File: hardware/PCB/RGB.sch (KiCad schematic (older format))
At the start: 26 parts, among them U1 IS31FL3733-QF, U2 IS31FL3733-QF

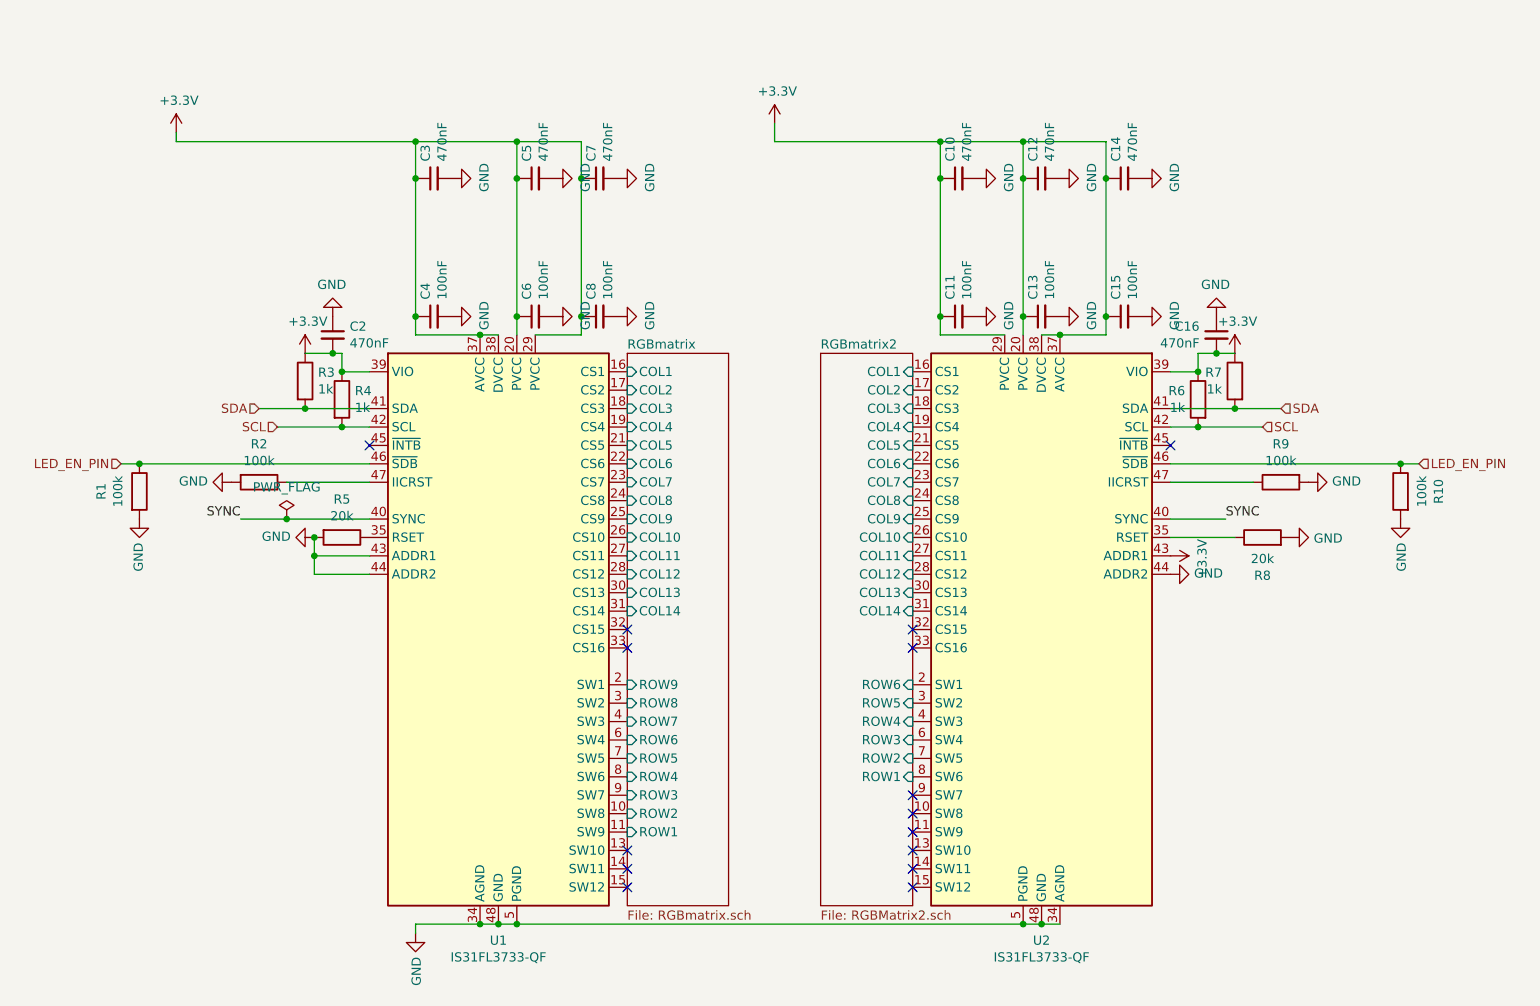
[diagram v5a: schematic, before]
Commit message: Use the correct Footprint
I think I can't do more things before the parts arrive and figure out what LED im going to use
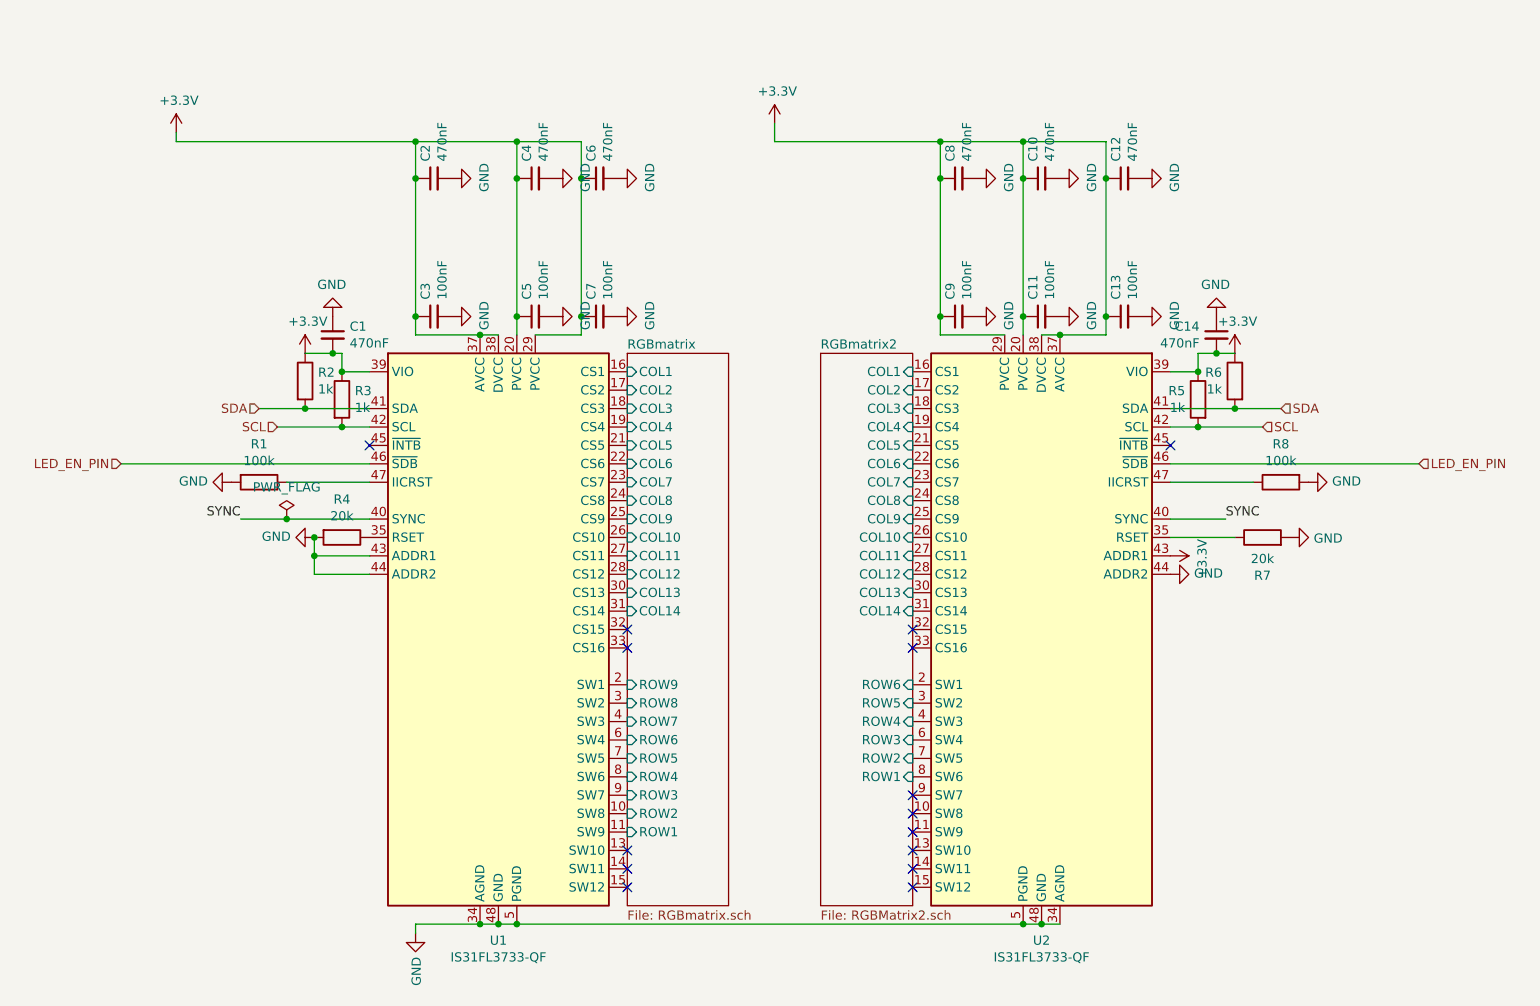
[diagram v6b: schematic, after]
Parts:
- removed R1, R10: 100k, Resistor_SMD:R_0402_1005Metric, symbol Device:R
- renumbered C2 to C1, C12 to C10, C13 to C11, C14 to C12, C15 to C13, C16 to C14, C3 to C2, C4 to C3, C5 to C4, C6 to C5, C7 to C6, C8 to C7, C10 to C8, C11 to C9, R2 to R1, R3 to R2, R4 to R3, R5 to R4, R6 to R5, R7 to R6, R8 to R7, R9 to R8

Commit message: alot of changes
modify the QFN-48 so PCB 3d view in future would look better (so I don't design a part that doesn't fit)
I made a useless QFN-40 3d model
modify schematics so it looks better
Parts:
- C1, C10, C12, C14, C2, C4, C6, C8: Footprint Capacitor_SMD:C_0603_1608Metric_Pad1.05x0.95mm_HandSolder -> Capacitor_SMD:C_0402_1005Metric; Value 0.47μF -> 470nF
- C11, C13, C3, C5, C7, C9: Footprint Capacitor_SMD:C_0603_1608Metric_Pad1.05x0.95mm_HandSolder -> Capacitor_SMD:C_0402_1005Metric; Value 0.1μF -> 100nf
- R1, R2, R3, R4, R5, R6, R7, R8: Footprint Resistor_SMD:R_0603_1608Metric_Pad1.05x0.95mm_HandSolder -> Resistor_SMD:R_0402_1005Metric
- U1, U2: footprint Package_DFN_QFN:QFN-48-1EP_6x6mm_P0.4mm_EP4.2x4.2mm_ThermalVias -> KiCad:QFN-48-1EP_6x6mm_P0.4mm_EP4.2x4.2mm_ThermalVias
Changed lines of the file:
@@
 encoding utf-8
 Sheet 3 6
-Title ""
-Date ""
-Rev ""
+Title "NHW68"
+Date "2020-01-28"
+Rev "0.1"
 Comp ""
 Comment1 ""
@@
 F 3 "~" H 8300 3100 50  0001 C CNN
 F 4 "20k" H 8300 3100 50  0001 C CNN "Value"
-F 5 "Resistor_SMD:R_0603_1608Metric_Pad1.05x0.95mm_HandSolder" H 8300 3100 50  0001 C CNN "Footprint"
+F 5 "Resistor_SMD:R_0402_1005Metric" H 8300 3100 50  0001 C CNN "Footprint"
 	1    8300 3100
 	0    -1   -1   0
@@
 F 3 "~" H 8400 2800 50  0001 C CNN
 F 4 "100k" H 8400 2800 50  0001 C CNN "Value"
-F 5 "Resistor_SMD:R_0603_1608Metric_Pad1.05x0.95mm_HandSolder" H 8400 2800 50  0001 C CNN "Footprint"
+F 5 "Resistor_SMD:R_0402_1005Metric" H 8400 2800 50  0001 C CNN "Footprint"
 	1    8400 2800
 	0    -1   1    0
@@
 F 2 "Capacitor_SMD:C_0402_1005Metric" H 8050 2000 50  0001 C CNN
 F 3 "~" H 8050 2000 50  0001 C CNN
-F 4 "Capacitor_SMD:C_0603_1608Metric_Pad1.05x0.95mm_HandSolder" H 8050 2000 50  0001 C CNN "Footprint"
-F 5 "0.47μF" H 8050 2000 50  0001 C CNN "Value"
+F 4 "Capacitor_SMD:C_0402_1005Metric" H 8050 2000 50  0001 C CNN "Footprint"
+F 5 "470nF" H 8050 2000 50  0001 C CNN "Value"
 	1    8050 2000
 	-1   0    0    -1
@@
 F 3 "~" H 7950 2350 50  0001 C CNN
 F 4 "1k" H 7950 2350 50  0001 C CNN "Value"
-F 5 "Resistor_SMD:R_0603_1608Metric_Pad1.05x0.95mm_HandSolder" H 7950 2350 50  0001 C CNN "Footprint"
+F 5 "Resistor_SMD:R_0402_1005Metric" H 7950 2350 50  0001 C CNN "Footprint"
 	1    7950 2350
 	-1   0    0    -1
@@
 F 3 "~" H 8150 2250 50  0001 C CNN
 F 4 "1k" H 8150 2250 50  0001 C CNN "Value"
-F 5 "Resistor_SMD:R_0603_1608Metric_Pad1.05x0.95mm_HandSolder" H 8150 2250 50  0001 C CNN "Footprint"
+F 5 "Resistor_SMD:R_0402_1005Metric" H 8150 2250 50  0001 C CNN "Footprint"
 	1    8150 2250
 	-1   0    0    -1
@@
 F 2 "Capacitor_SMD:C_0402_1005Metric" H 3250 2000 50  0001 C CNN
 F 3 "~" H 3250 2000 50  0001 C CNN
-F 4 "Capacitor_SMD:C_0603_1608Metric_Pad1.05x0.95mm_HandSolder" H 3250 2000 50  0001 C CNN "Footprint"
-F 5 "0.47μF" H 3250 2000 50  0001 C CNN "Value"
+F 4 "Capacitor_SMD:C_0402_1005Metric" H 3250 2000 50  0001 C CNN "Footprint"
+F 5 "470nF" H 3250 2000 50  0001 C CNN "Value"
 	1    3250 2000
 	1    0    0    -1
@@
 F 3 "~" H 3300 3100 50  0001 C CNN
 F 4 "20k" H 3300 3100 50  0001 C CNN "Value"
-F 5 "Resistor_SMD:R_0603_1608Metric_Pad1.05x0.95mm_HandSolder" H 3300 3100 50  0001 C CNN "Footprint"
+F 5 "Resistor_SMD:R_0402_1005Metric" H 3300 3100 50  0001 C CNN "Footprint"
 	1    3300 3100
 	0    1    1    0
@@
 F 3 "~" H 3300 2350 50  0001 C CNN
 F 4 "1k" H 3300 2350 50  0001 C CNN "Value"
-F 5 "Resistor_SMD:R_0603_1608Metric_Pad1.05x0.95mm_HandSolder" H 3300 2350 50  0001 C CNN "Footprint"
+F 5 "Resistor_SMD:R_0402_1005Metric" H 3300 2350 50  0001 C CNN "Footprint"
 	1    3300 2350
 	1    0    0    -1
@@
 F 3 "~" H 3100 2250 50  0001 C CNN
 F 4 "1k" H 3100 2250 50  0001 C CNN "Value"
-F 5 "Resistor_SMD:R_0603_1608Metric_Pad1.05x0.95mm_HandSolder" H 3100 2250 50  0001 C CNN "Footprint"
+F 5 "Resistor_SMD:R_0402_1005Metric" H 3100 2250 50  0001 C CNN "Footprint"
 	1    3100 2250
 	1    0    0    -1
@@
 F 3 "~" H 2850 2800 50  0001 C CNN
 F 4 "100k" H 2850 2800 50  0001 C CNN "Value"
-F 5 "Resistor_SMD:R_0603_1608Metric_Pad1.05x0.95mm_HandSolder" H 2850 2800 50  0001 C CNN "Footprint"
+F 5 "Resistor_SMD:R_0402_1005Metric" H 2850 2800 50  0001 C CNN "Footprint"
 	1    2850 2800
 	0    1    1    0
@@
 F 0 "U2" H 7100 1911 50  0000 C CNN
 F 1 "IS31FL3733-QF" H 7100 1820 50  0000 C CNN
-F 2 "Package_DFN_QFN:QFN-48-1EP_6x6mm_P0.4mm_EP4.2x4.2mm_ThermalVias" H 7100 3600 50  0001 C CNN
+F 2 "KiCad:QFN-48-1EP_6x6mm_P0.4mm_EP4.2x4.2mm_ThermalVias" H 7100 3600 50  0001 C CNN
 F 3 "http://www.issi.com/WW/pdf/IS31FL3733.pdf" H 7100 3600 50  0001 C CNN
 F 4 "IS31FL7377" H 7100 3600 50  0001 C CNN "Value"
@@
 F 0 "U1" H 4150 1911 50  0000 C CNN
 F 1 "IS31FL3733-QF" H 4150 1820 50  0000 C CNN
-F 2 "Package_DFN_QFN:QFN-48-1EP_6x6mm_P0.4mm_EP4.2x4.2mm_ThermalVias" H 4150 3600 50  0001 C CNN
+F 2 "KiCad:QFN-48-1EP_6x6mm_P0.4mm_EP4.2x4.2mm_ThermalVias" H 4150 3600 50  0001 C CNN
 F 3 "http://www.issi.com/WW/pdf/IS31FL3733.pdf" H 4150 3600 50  0001 C CNN
 F 4 "IS31FL7377" H 4150 3600 50  0001 C CNN "Value"
@@
 F 2 "Capacitor_SMD:C_0402_1005Metric" H 7100 1900 50  0001 C CNN
 F 3 "~" H 7100 1900 50  0001 C CNN
-F 4 "Capacitor_SMD:C_0603_1608Metric_Pad1.05x0.95mm_HandSolder" H 7100 1900 50  0001 C CNN "Footprint"
-F 5 "0.1μF" H 7100 1900 50  0001 C CNN "Value"
+F 4 "Capacitor_SMD:C_0402_1005Metric" H 7100 1900 50  0001 C CNN "Footprint"
+F 5 "100nf" H 7100 1900 50  0001 C CNN "Value"
 	1    7100 1900
 	0    -1   -1   0
@@
 F 2 "Capacitor_SMD:C_0402_1005Metric" H 7100 1150 50  0001 C CNN
 F 3 "~" H 7100 1150 50  0001 C CNN
-F 4 "Capacitor_SMD:C_0603_1608Metric_Pad1.05x0.95mm_HandSolder" H 7100 1150 50  0001 C CNN "Footprint"
-F 5 "0.47μF" H 7100 1150 50  0001 C CNN "Value"
+F 4 "Capacitor_SMD:C_0402_1005Metric" H 7100 1150 50  0001 C CNN "Footprint"
+F 5 "470nF" H 7100 1150 50  0001 C CNN "Value"
 	1    7100 1150
 	0    -1   -1   0
@@
 F 2 "Capacitor_SMD:C_0402_1005Metric" H 6650 1900 50  0001 C CNN
 F 3 "~" H 6650 1900 50  0001 C CNN
-F 4 "Capacitor_SMD:C_0603_1608Metric_Pad1.05x0.95mm_HandSolder" H 6650 1900 50  0001 C CNN "Footprint"
-F 5 "0.1μF" H 6650 1900 50  0001 C CNN "Value"
+F 4 "Capacitor_SMD:C_0402_1005Metric" H 6650 1900 50  0001 C CNN "Footprint"
+F 5 "100nf" H 6650 1900 50  0001 C CNN "Value"
 	1    6650 1900
 	0    -1   -1   0
@@
 F 2 "Capacitor_SMD:C_0402_1005Metric" H 6650 1150 50  0001 C CNN
 F 3 "~" H 6650 1150 50  0001 C CNN
-F 4 "Capacitor_SMD:C_0603_1608Metric_Pad1.05x0.95mm_HandSolder" H 6650 1150 50  0001 C CNN "Footprint"
-F 5 "0.47μF" H 6650 1150 50  0001 C CNN "Value"
+F 4 "Capacitor_SMD:C_0402_1005Metric" H 6650 1150 50  0001 C CNN "Footprint"
+F 5 "470nF" H 6650 1150 50  0001 C CNN "Value"
 	1    6650 1150
 	0    -1   -1   0
@@
 F 2 "Capacitor_SMD:C_0402_1005Metric" H 7550 1900 50  0001 C CNN
 F 3 "~" H 7550 1900 50  0001 C CNN
-F 4 "Capacitor_SMD:C_0603_1608Metric_Pad1.05x0.95mm_HandSolder" H 7550 1900 50  0001 C CNN "Footprint"
-F 5 "0.1μF" H 7550 1900 50  0001 C CNN "Value"
+F 4 "Capacitor_SMD:C_0402_1005Metric" H 7550 1900 50  0001 C CNN "Footprint"
+F 5 "100nf" H 7550 1900 50  0001 C CNN "Value"
 	1    7550 1900
 	0    -1   -1   0
@@
 F 2 "Capacitor_SMD:C_0402_1005Metric" H 7550 1150 50  0001 C CNN
 F 3 "~" H 7550 1150 50  0001 C CNN
-F 4 "Capacitor_SMD:C_0603_1608Metric_Pad1.05x0.95mm_HandSolder" H 7550 1150 50  0001 C CNN "Footprint"
-F 5 "0.47μF" H 7550 1150 50  0001 C CNN "Value"
+F 4 "Capacitor_SMD:C_0402_1005Metric" H 7550 1150 50  0001 C CNN "Footprint"
+F 5 "470nF" H 7550 1150 50  0001 C CNN "Value"
 	1    7550 1150
 	0    -1   -1   0
@@
 F 2 "Capacitor_SMD:C_0402_1005Metric" H 4350 1900 50  0001 C CNN
 F 3 "~" H 4350 1900 50  0001 C CNN
-F 4 "Capacitor_SMD:C_0603_1608Metric_Pad1.05x0.95mm_HandSolder" H 4350 1900 50  0001 C CNN "Footprint"
-F 5 "0.1μF" H 4350 1900 50  0001 C CNN "Value"
+F 4 "Capacitor_SMD:C_0402_1005Metric" H 4350 1900 50  0001 C CNN "Footprint"
+F 5 "100nf" H 4350 1900 50  0001 C CNN "Value"
 	1    4350 1900
 	0    -1   -1   0
@@
 F 2 "Capacitor_SMD:C_0402_1005Metric" H 4350 1150 50  0001 C CNN
 F 3 "~" H 4350 1150 50  0001 C CNN
-F 4 "Capacitor_SMD:C_0603_1608Metric_Pad1.05x0.95mm_HandSolder" H 4350 1150 50  0001 C CNN "Footprint"
-F 5 "0.47μF" H 4350 1150 50  0001 C CNN "Value"
+F 4 "Capacitor_SMD:C_0402_1005Metric" H 4350 1150 50  0001 C CNN "Footprint"
+F 5 "470nF" H 4350 1150 50  0001 C CNN "Value"
 	1    4350 1150
 	0    -1   -1   0
@@
 F 2 "Capacitor_SMD:C_0402_1005Metric" H 3800 1900 50  0001 C CNN
 F 3 "~" H 3800 1900 50  0001 C CNN
-F 4 "Capacitor_SMD:C_0603_1608Metric_Pad1.05x0.95mm_HandSolder" H 3800 1900 50  0001 C CNN "Footprint"
-F 5 "0.1μF" H 3800 1900 50  0001 C CNN "Value"
+F 4 "Capacitor_SMD:C_0402_1005Metric" H 3800 1900 50  0001 C CNN "Footprint"
+F 5 "100nf" H 3800 1900 50  0001 C CNN "Value"
 	1    3800 1900
 	0    -1   -1   0
@@
 F 2 "Capacitor_SMD:C_0402_1005Metric" H 3800 1150 50  0001 C CNN
 F 3 "~" H 3800 1150 50  0001 C CNN
-F 4 "Capacitor_SMD:C_0603_1608Metric_Pad1.05x0.95mm_HandSolder" H 3800 1150 50  0001 C CNN "Footprint"
-F 5 "0.47μF" H 3800 1150 50  0001 C CNN "Value"
+F 4 "Capacitor_SMD:C_0402_1005Metric" H 3800 1150 50  0001 C CNN "Footprint"
+F 5 "470nF" H 3800 1150 50  0001 C CNN "Value"
 	1    3800 1150
 	0    -1   -1   0
@@
 F 2 "Capacitor_SMD:C_0402_1005Metric" H 4700 1900 50  0001 C CNN
 F 3 "~" H 4700 1900 50  0001 C CNN
-F 4 "Capacitor_SMD:C_0603_1608Metric_Pad1.05x0.95mm_HandSolder" H 4700 1900 50  0001 C CNN "Footprint"
-F 5 "0.1μF" H 4700 1900 50  0001 C CNN "Value"
+F 4 "Capacitor_SMD:C_0402_1005Metric" H 4700 1900 50  0001 C CNN "Footprint"
+F 5 "100nf" H 4700 1900 50  0001 C CNN "Value"
 	1    4700 1900
 	0    -1   -1   0
@@
 F 2 "Capacitor_SMD:C_0402_1005Metric" H 4700 1150 50  0001 C CNN
 F 3 "~" H 4700 1150 50  0001 C CNN
-F 4 "Capacitor_SMD:C_0603_1608Metric_Pad1.05x0.95mm_HandSolder" H 4700 1150 50  0001 C CNN "Footprint"
-F 5 "0.47μF" H 4700 1150 50  0001 C CNN "Value"
+F 4 "Capacitor_SMD:C_0402_1005Metric" H 4700 1150 50  0001 C CNN "Footprint"
+F 5 "470nF" H 4700 1150 50  0001 C CNN "Value"
 	1    4700 1150
 	0    -1   -1   0

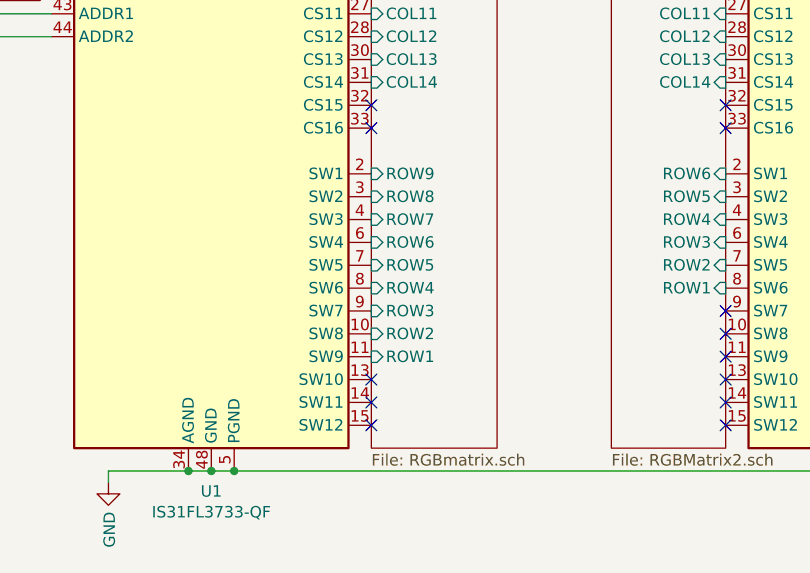
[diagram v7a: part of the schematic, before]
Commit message: Connecting RGBs
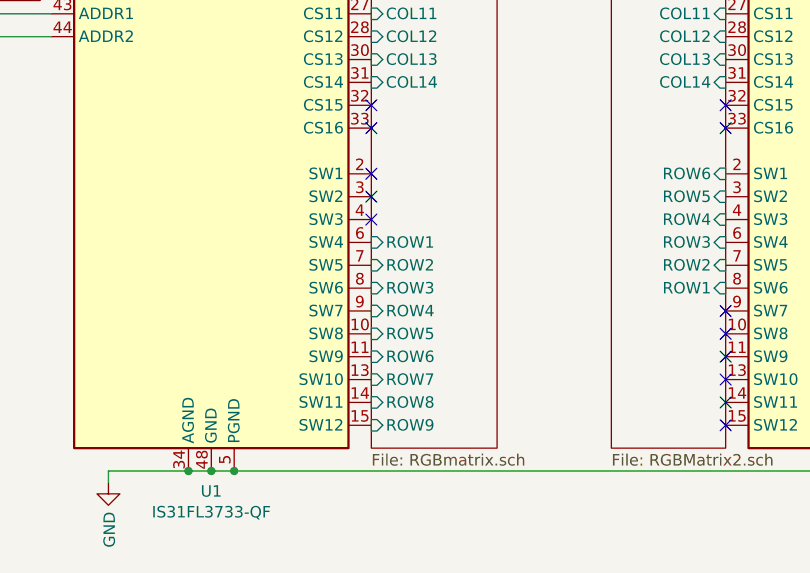
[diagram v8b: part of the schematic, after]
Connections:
- net RGBmatrix/ROW1: now also U1.6 (SW4); no longer U1.11 (SW9)
- net RGBmatrix/ROW2: now also U1.7 (SW5); no longer U1.10 (SW8)
- net RGBmatrix/ROW3: now also U1.8 (SW6); no longer U1.9 (SW7)
- net RGBmatrix/ROW4: now also U1.9 (SW7); no longer U1.8 (SW6)
- net RGBmatrix/ROW5: now also U1.10 (SW8); no longer U1.7 (SW5)
- net RGBmatrix/ROW6: now also U1.11 (SW9); no longer U1.6 (SW4)
- net RGBmatrix/ROW7: now also U1.13 (SW10); no longer U1.4 (SW3)
- net RGBmatrix/ROW8: now also U1.14 (SW11); no longer U1.3 (SW2)
- net RGBmatrix/ROW9: now also U1.15 (SW12); no longer U1.2 (SW1)
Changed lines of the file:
@@
 F21 "ROW6" I R 6400 3900 50
 $EndSheet
-NoConn ~ 4850 5000
-NoConn ~ 4850 4900
-NoConn ~ 4850 4800
 Wire Wire Line
 	3250 2100 3300 2100
@@
 F14 "COL13" I L 4850 3400 50
 F15 "COL14" I L 4850 3500 50
-F16 "ROW1" I L 4850 4700 50
-F17 "ROW2" I L 4850 4600 50
-F18 "ROW3" I L 4850 4500 50
-F19 "ROW4" I L 4850 4400 50
-F20 "ROW5" I L 4850 4300 50
-F21 "ROW6" I L 4850 4200 50
-F22 "ROW7" I L 4850 4100 50
-F23 "ROW8" I L 4850 4000 50
-F24 "ROW9" I L 4850 3900 50
+F16 "ROW1" I L 4850 4200 50
+F17 "ROW2" I L 4850 4300 50
+F18 "ROW3" I L 4850 4400 50
+F19 "ROW4" I L 4850 4500 50
+F20 "ROW5" I L 4850 4600 50
+F21 "ROW6" I L 4850 4700 50
+F22 "ROW7" I L 4850 4800 50
+F23 "ROW8" I L 4850 4900 50
+F24 "ROW9" I L 4850 5000 50
 $EndSheet
 $Comp
@@
 Wire Wire Line
 	2100 2700 3450 2700
+NoConn ~ 4850 4100
+NoConn ~ 4850 4000
+NoConn ~ 4850 3900
 $EndSCHEMATC
